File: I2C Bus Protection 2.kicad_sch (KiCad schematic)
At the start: 18 parts, among them Q10 MBT2222ADW1T1, Q11 NX3008NBKS, Q12 MBT2222ADW1T1, Q9 NX3008NBKS

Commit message: Layout mostly complete
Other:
- title: (none) -> Argus Reaction Wheel
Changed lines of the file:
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@@
 	(generator_version "8.0")
 	(paper "A4")
+	(title_block
+		(title "Argus Reaction Wheel")
+		(date "2025-03-24")
+		(rev "1.0")
+	)
 	(junction
 		(at 100.33 68.58)

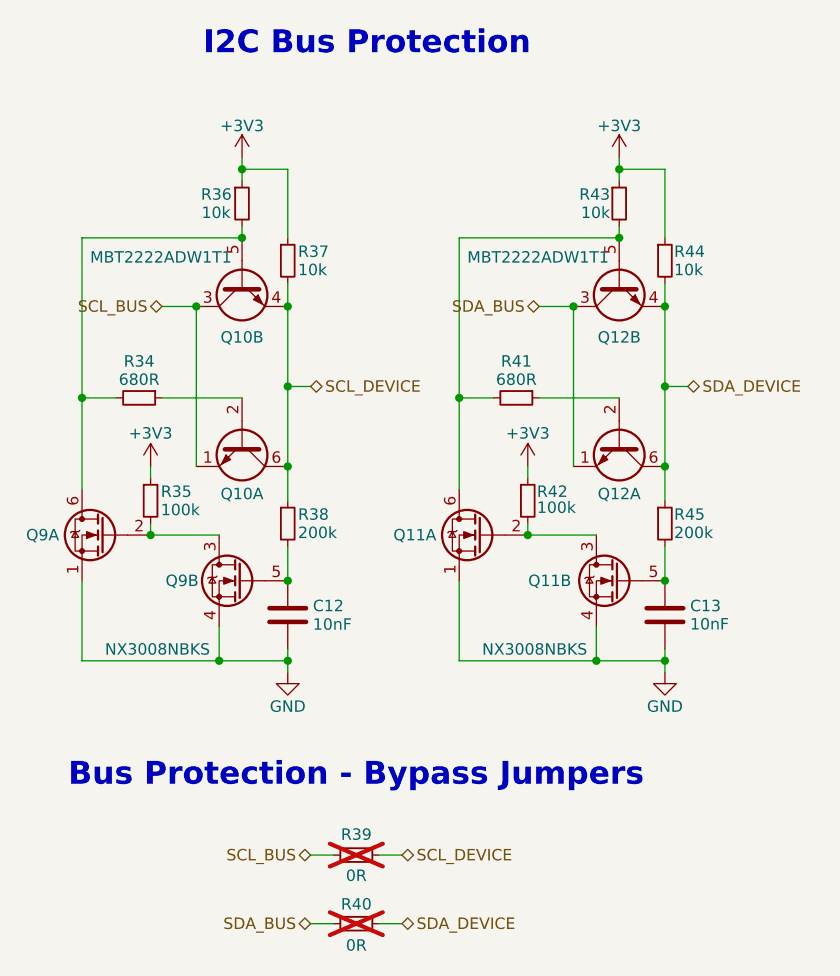
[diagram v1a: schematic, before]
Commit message: Add and correct BOM for easy Digikey ordering
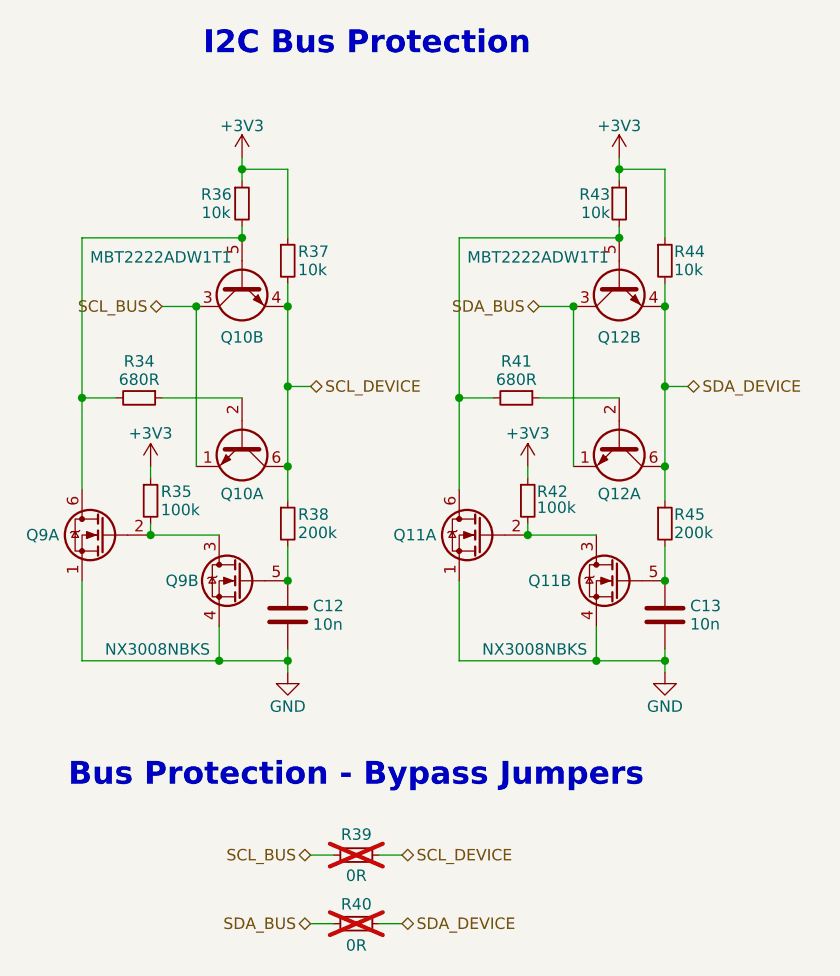
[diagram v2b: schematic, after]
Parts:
- C12, C13: value 10nF -> 10n; Digikey (none) -> https://www.digikey.com/en/products/detail/samsung-electro-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; Digikey PN (none) -> 490-4934-1-ND; MPN (none) -> CL10B103KO8WPNC; Part (none) -> CL10B103KO8WPNC
- Q10, Q12: Digikey (none) -> https://www.digikey.com/en/products/detail/onsemi/MBT2222AD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; Digikey PN (none) -> MBT2222ADW1T1GOSCT-ND; MPN (none) -> MBT2222ADW1T1G; Part (none) -> MBT2222ADW1T1G
- Q11, Q9: Digikey (none) -> https://www.digikey.com/en/products/detail/nexperia-usa-inc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; Digikey PN (none) -> 1727-1221-1-ND; MPN (none) -> NX3008NBKS,115; Part (none) -> NX3008NBKS,115
- R34, R41: Digikey (none) -> https://www.digikey.com/en/products/detail/yageo/RC0603FR-0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; Digikey PN (none) -> 311-680HRCT-ND; MPN (none) -> RC0603FR-07680RL; Part (none) -> RC0603FR-07680RL
- R35, R42: Digikey (none) -> https://www.digikey.com/en/products/detail/yageo/RC0603FR-0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; Digikey PN (none) -> 311-100KHRCT-ND; MPN (none) -> RC0603FR-07100KL; Part (none) -> RC0603FR-07100KL
- R36, R37, R43, R44: Digikey (none) -> https://www.digikey.com/en/products/detail/yageo/RC0603FR-0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; Digikey PN (none) -> 311-10.0KHRCT-ND; MPN (none) -> RC0603FR-0710KL; Part (none) -> RC0603FR-0710KL
- R38, R45: Digikey (none) -> https://www.digikey.com/en/products/detail/yageo/RC0603FR-0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; Digikey PN (none) -> 311-200KHRCT-ND; MPN (none) -> RC0603FR-07200KL; Part (none) -> RC0603FR-07200KL
- R39, R40: Digikey (none) -> https://www.digikey.com/en/products/detail/bourns-inc/CR060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; Digikey PN (none) -> CR0603-J/-000ELFCT-ND; MPN (none) -> CR0603-J/-000ELF; Part (none) -> CR0603-J/-000ELF
